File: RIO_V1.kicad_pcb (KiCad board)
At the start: 2 copper layers, 43.1 x 43.1 mm, 3 parts, among them J1 Conn_01x13_Pin, U1 TinyS3_Symbol

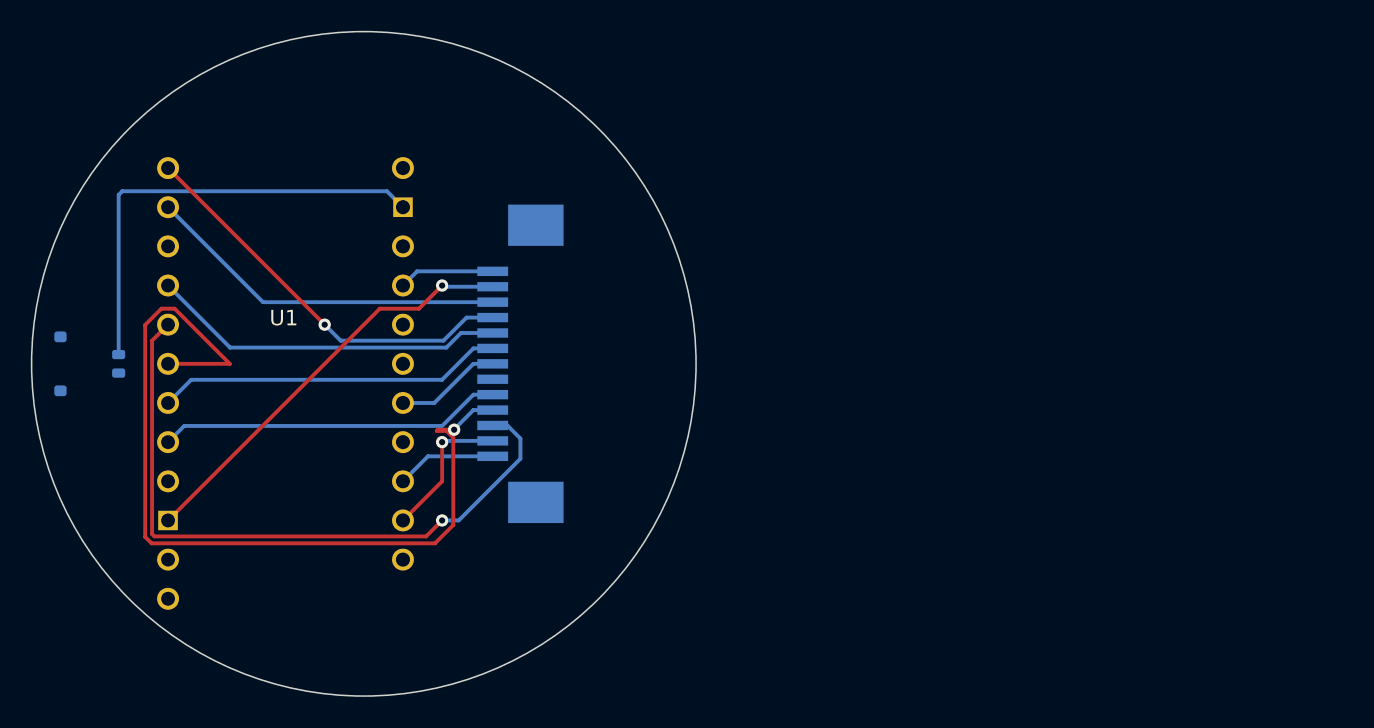
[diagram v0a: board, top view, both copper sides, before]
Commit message: Updated Schematics & PCB To Incorporate Connector
Updated Schematic and PVB to incorporate the JST Connector instead of resodering it with a TE FPC connector
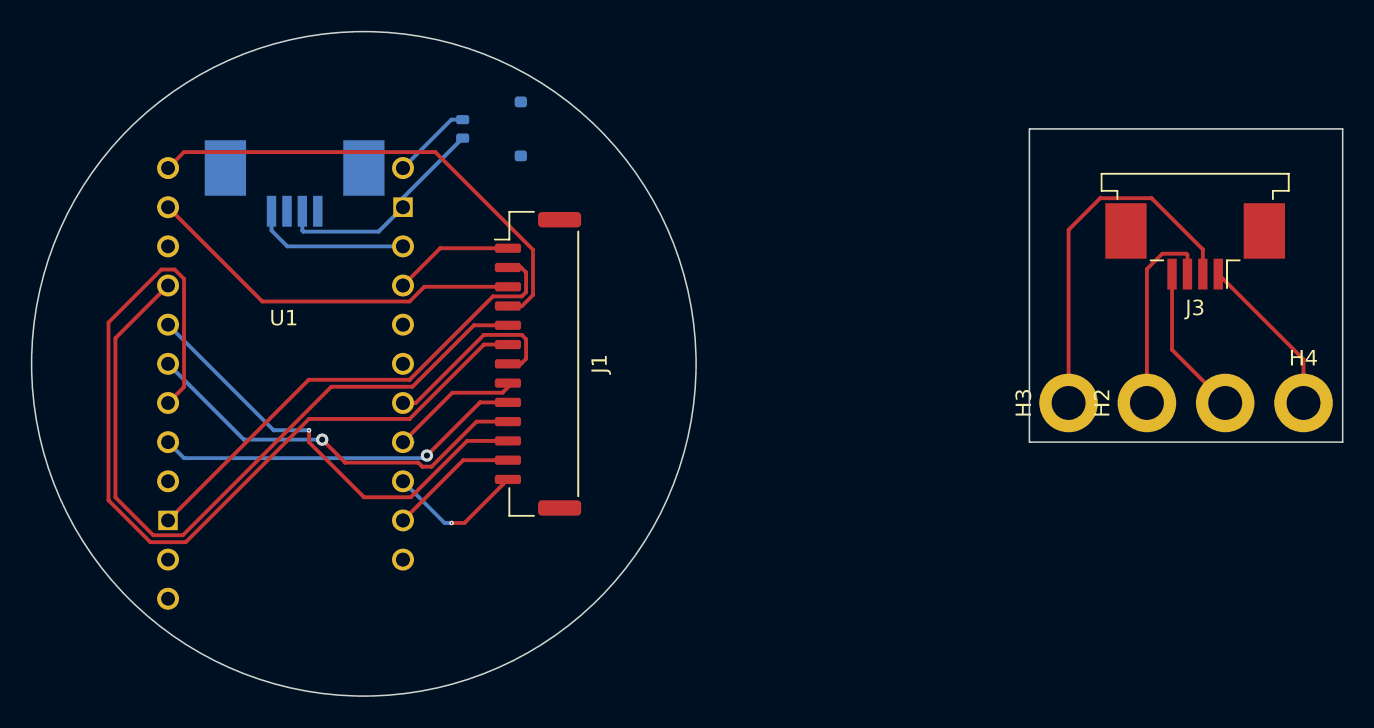
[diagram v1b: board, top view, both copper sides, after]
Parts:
- added H1: Pin_2, MountingHole:MountingHole_2.2mm_M2_DIN965_Pad, F.Cu at (221.0, 96.5)
- added H2: Pin_3, MountingHole:MountingHole_2.2mm_M2_DIN965_Pad, F.Cu at (215.9, 96.5)
- added H3: Pin_4, MountingHole:MountingHole_2.2mm_M2_DIN965_Pad, F.Cu at (210.8, 96.5)
- added H4: Pin_4, MountingHole:MountingHole_2.2mm_M2_DIN965_Pad, F.Cu at (226.1, 96.5)
- added J2: Conn_01x03_Pin, Connector_FFC-FPC:TE_84952-4_1x04-1MP_P1.0mm_Horizontal, B.Cu at (160.6, 82.3)
- added J3: Conn_01x04_Pin, Connector_FFC-FPC:TE_84952-4_1x04-1MP_P1.0mm_Horizontal, F.Cu at (219.0, 86.4)
- J1: footprint Connector_FFC-FPC:TE_1-84953-3_1x13-1MP_P1.0mm_Horizontal -> Connector_JST:JST_GH_BM13B-GHS-TBT_1x13-1MP_P1.25mm_Vertical; moved to F.Cu
- moved BT1 30.2 mm to (173.4, 78.7), turned to -90 degrees
- moved J1 1.14 mm to (176.4, 94.0)
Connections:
- net -BATT renamed Net-(BT1--)
- U1 pad 3: +BATT -> Net-(J2-Pin_1)
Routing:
- net Net-(J1-Pin_6): track 22.5 -> 58.9 mm
- net Net-(J1-Pin_10): track 57.0 -> 26.0 mm
- net Net-(J1-Pin_5): track 23.1 -> 47.3 mm
- net Net-(J3-Pin_2): track 0.00 -> 23.8 mm
- net Net-(J1-Pin_11): track 43.5 -> 28.7 mm
- net Net-(BT1--): track 29.3 -> 14.6 mm
- net Net-(J3-Pin_3): track 0.00 -> 13.0 mm
- net Net-(J3-Pin_1): track 0.00 -> 10.7 mm
- net Net-(J2-Pin_1): track 0.00 -> 10.2 mm
- net Net-(J3-Pin_4): track 0.00 -> 9.79 mm
- net Net-(J1-Pin_8): track 0.00 -> 9.58 mm
- net Net-(J1-Pin_7): track 6.87 -> 12.5 mm
- net Net-(J1-Pin_4): track 26.3 -> 31.6 mm, vias 1 -> 0
- net Net-(BT1-+): track 0.00 -> 5.17 mm
- net Net-(J1-Pin_2): track 27.4 -> 31.9 mm, vias 1 -> 0
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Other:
- board size 43.1 x 43.1 mm -> 85.1 x 43.1 mm
